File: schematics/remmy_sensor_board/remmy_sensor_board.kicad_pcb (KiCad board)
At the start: 2 copper layers, 30 x 50 mm, 21 parts, among them J2 Conn_02x05_Counter_Clockwise, J3 USB_C_Receptacle_USB2.0_14P, U1 AP2112K-3.3TRG1, U2 USBLC6-2SC6, U3 TPS73219DBVT, U5 PMW3360DM-T2QU

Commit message: added images
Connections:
- U1 pad 3: unconnected-(U1-EN-Pad3) -> +5V
- U3 pad 3: unconnected-(U3-EN-Pad3) -> +3.3V
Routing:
- net +5V: track 27.1 -> 30.6 mm
- net +3.3V: track 47.7 -> 50.9 mm
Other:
- board text added: "Remmy v2.1B"
- board text removed: "Remmy v2.0B"

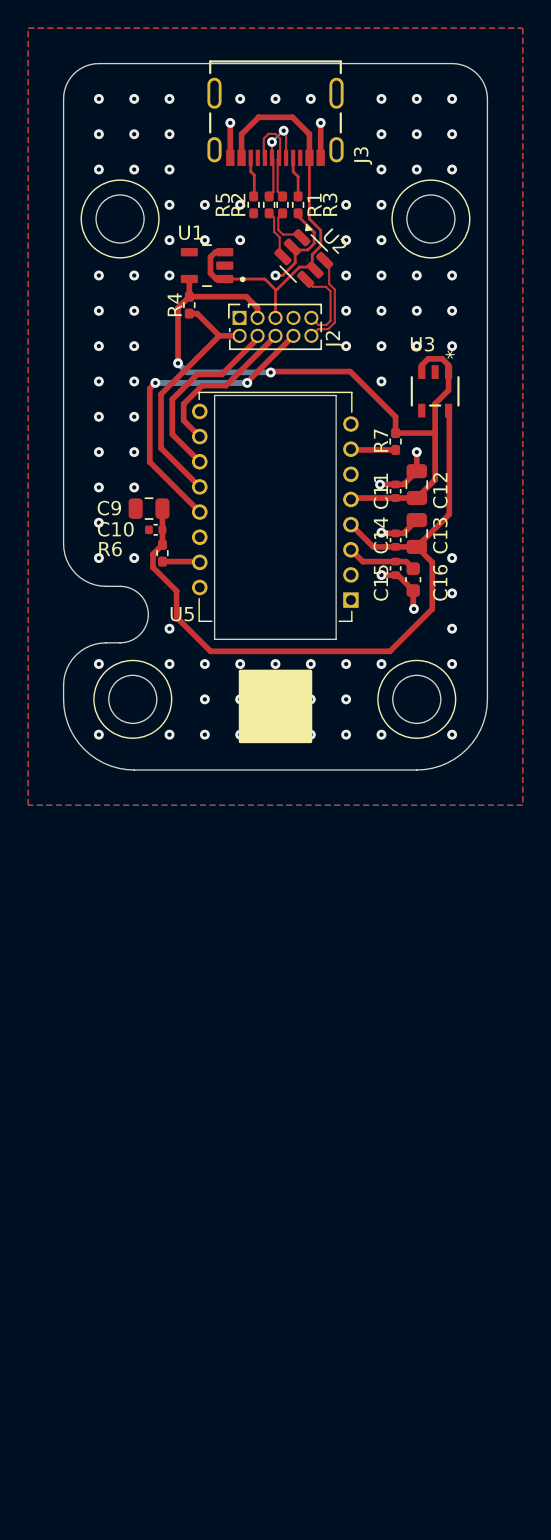
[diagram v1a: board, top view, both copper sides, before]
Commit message: broken spi comm
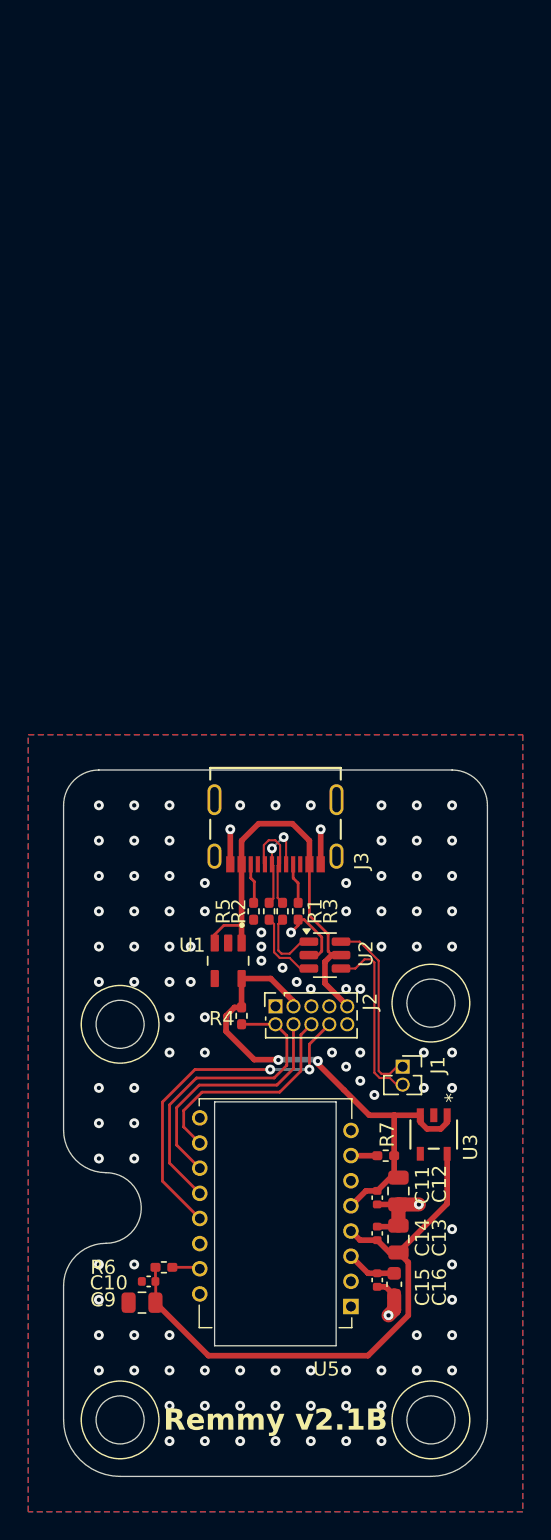
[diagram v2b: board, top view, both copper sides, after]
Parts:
- added J1: Conn_01x02, Connector_PinSocket_1.27mm:PinSocket_1x02_P1.27mm_Vertical, F.Cu at (124.0, 121.0)
- moved C9 56.2 mm to (105.6, 137.7)
- moved C10 53.2 mm to (106.0, 136.2)
- moved U3 52.6 mm to (126.2, 125.8)
- moved R7 50.6 mm to (122.8, 127.3), turned to 180 degrees
- moved R6 50.5 mm to (107.1, 135.2), turned to 0 degrees
- moved R4 50.4 mm to (112.6, 117.4)
- moved C15 50.4 mm to (122.2, 136.1)
- moved C11 50.0 mm to (122.2, 130.3), turned to -90 degrees
- moved C12 50.0 mm to (123.7, 129.8), turned to -90 degrees
- moved J3 50.0 mm to (115.0, 103.2)
- moved R1 50.0 mm to (115.5, 110.0)
- moved R2 50.0 mm to (114.5, 110.0)
- moved R3 50.0 mm to (116.6, 110.0)
- moved R5 50.0 mm to (113.5, 110.0)
- moved U5 50.0 mm to (120.3, 138.0)
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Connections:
- J2 pad 3: +5V -> GND
- J2 pad 5: Net-(J2-Pin_5) -> +5V
- J2 pad 6: Net-(J2-Pin_6) -> GND
- U2 pad 4: Net-(J2-Pin_5) -> Net-(J1-Pin_2)
- U2 pad 6: Net-(J2-Pin_6) -> Net-(J1-Pin_1)
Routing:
- net +3.3V: track 50.9 -> 37.6 mm
- net Net-(J1-Pin_1): track 0.00 -> 13.0 mm
- net Net-(J1-Pin_2): track 0.00 -> 12.9 mm
- net +1.9V: track 49.8 -> 40.3 mm
- net Net-(J2-Pin_6): track 6.74 -> 0.00 mm
- net Net-(J2-Pin_5): track 5.89 -> 0.00 mm
- net Net-(J2-Pin_8): track 11.3 -> 15.8 mm
- net GND: track 23.8 -> 19.3 mm, vias 97 -> 110
- net Net-(J2-Pin_10): track 17.8 -> 22.2 mm
- net Net-(J2-Pin_9): track 13.2 -> 17.5 mm
- net Net-(J2-Pin_7): track 22.0 -> 24.5 mm
- net Net-(R2-Pad1): track 3.70 -> 5.61 mm
- net Net-(R1-Pad1): track 3.39 -> 5.11 mm
- net Net-(U5-VDDPIX): track 4.96 -> 3.56 mm
- net Net-(U5-NRESET): track 3.18 -> 1.87 mm
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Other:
- outline, holes or cut-outs redrawn
